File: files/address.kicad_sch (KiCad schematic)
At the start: 4 parts, among them J1 VLB_slot, U1 86C325

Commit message: initial PCB routed
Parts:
- added C14: 0.1uF, Capacitor_SMD:C_0805_2012Metric_Pad1.18x1.45mm_HandSolder, symbol Device:C
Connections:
- net GND: now also C14.2
- net at R5.1, U1.193 (~{SRESET}): now also C14.1
- net IRQ2: no longer names the net of JP2.1 (Pin_1)
- no-connect marks 8 -> 9
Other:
- moved on the sheet: R5
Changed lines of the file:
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@@
 (kicad_sch (version 20230121) (generator eeschema)
   (paper "A4")
+  (junction (at 190.5 133.35) (diameter 0) (color 0 0 0 0)
+  )
   (no_connect (at 39.37 85.09))
   (no_connect (at 72.39 85.09))
@@
   (no_connect (at 66.04 187.96))
   (no_connect (at 57.15 85.09))
+  (no_connect (at 191.77 100.33))
   (wire (pts (xy 20.32 130.81) (xy 27.94 130.81))
     (stroke (width 0) (type default))
@@
     (stroke (width 0) (type default))
   )
+  (wire (pts (xy 190.5 133.35) (xy 190.5 137.16))
+    (stroke (width 0) (type default))
+  )
   (wire (pts (xy 158.75 182.88) (xy 149.86 182.88))
     (stroke (width 0) (type default))
@@
     (stroke (width 0) (type default))
   )
-  (wire (pts (xy 193.04 133.35) (xy 201.93 133.35))
+  (wire (pts (xy 186.69 133.35) (xy 190.5 133.35))
     (stroke (width 0) (type default))
   )
@@
     (stroke (width 0) (type default))
   )
-  (wire (pts (xy 185.42 100.33) (xy 191.77 100.33))
-    (stroke (width 0) (type default))
-  )
   (wire (pts (xy 158.75 185.42) (xy 149.86 185.42))
     (stroke (width 0) (type default))
@@
     (stroke (width 0) (type default))
   )
-  (wire (pts (xy 177.8 133.35) (xy 185.42 133.35))
+  (wire (pts (xy 171.45 133.35) (xy 179.07 133.35))
     (stroke (width 0) (type default))
   )
@@
     (stroke (width 0) (type default))
   )
+  (wire (pts (xy 190.5 133.35) (xy 201.93 133.35))
+    (stroke (width 0) (type default))
+  )
   (wire (pts (xy 67.31 80.01) (xy 67.31 85.09))
     (stroke (width 0) (type default))
@@
     (effects (font (size 1.27 1.27)) (justify right bottom))
   )
-  (label "RST" (at 177.8 133.35 0) (fields_autoplaced)
+  (label "RST" (at 171.45 133.35 0) (fields_autoplaced)
     (effects (font (size 1.27 1.27)) (justify left bottom))
   )
@@
     (effects (font (size 1.27 1.27)) (justify right bottom))
   )
-  (hierarchical_label "IRQ2" (shape input) (at 185.42 100.33 180) (fields_autoplaced)
-    (effects (font (size 1.27 1.27)) (justify right))
-  )
-  (symbol (lib_id "Device:R") (at 189.23 133.35 270) (mirror x) (unit 1)
+  (symbol (lib_id "Device:R") (at 182.88 133.35 270) (mirror x) (unit 1)
     (in_bom yes) (on_board yes) (dnp no)
-    (property "Reference" "R5" (at 187.96 128.27 90)
+    (property "Reference" "R5" (at 181.61 128.27 90)
       (effects (font (size 1.27 1.27)) (justify left))
     )
-    (property "Value" "100R" (at 187.325 130.81 90)
+    (property "Value" "100R" (at 180.975 130.81 90)
       (effects (font (size 1.27 1.27)) (justify left))
     )
-    (property "Footprint" "Resistor_SMD:R_0805_2012Metric_Pad1.20x1.40mm_HandSolder" (at 189.23 135.128 90)
+    (property "Footprint" "Resistor_SMD:R_0805_2012Metric_Pad1.20x1.40mm_HandSolder" (at 182.88 135.128 90)
       (effects (font (size 1.27 1.27)) hide)
     )
-    (property "Datasheet" "~" (at 189.23 133.35 0)
+    (property "Datasheet" "~" (at 182.88 133.35 0)
       (effects (font (size 1.27 1.27)) hide)
     )
@@
     )
   )
+  (symbol (lib_id "Device:C") (at 190.5 140.97 0) (unit 1)
+    (in_bom yes) (on_board yes) (dnp no)
+    (property "Reference" "C14" (at 184.15 138.43 0)
+      (effects (font (size 1.27 1.27)) (justify left))
+    )
+    (property "Value" "0.1uF" (at 182.88 143.51 0)
+      (effects (font (size 1.27 1.27)) (justify left))
+    )
+    (property "Footprint" "Capacitor_SMD:C_0805_2012Metric_Pad1.18x1.45mm_HandSolder" (at 191.4652 144.78 0)
+      (effects (font (size 1.27 1.27)) hide)
+    )
+    (property "Datasheet" "~" (at 190.5 140.97 0)
+      (effects (font (size 1.27 1.27)) hide)
+    )
+    (pin "1")
+    (pin "2")
+    (instances
+      (project "virge-vlb"
+        (path "/e8216711-86b5-4276-82f4-4c7ed22b9a9c"
+          (reference "C14") (unit 1)
+        )
+        (path "/e8216711-86b5-4276-82f4-4c7ed22b9a9c/9321f466-5ac6-411a-b039-07fb7f0cdeaa"
+          (reference "C15") (unit 1)
+        )
+      )
+    )
+  )
   (symbol (lib_id "power:GND") (at 27.94 179.07 0) (unit 1)
     (in_bom yes) (on_board yes) (dnp no) (fields_autoplaced)
@@
         )
       )
+    )
+  )
+  (symbol (lib_id "power:GND") (at 190.5 144.78 0) (unit 1)
+    (in_bom yes) (on_board yes) (dnp no) (fields_autoplaced)
+    (property "Reference" "#PWR05" (at 190.5 151.13 0)
+      (effects (font (size 1.27 1.27)) hide)
+    )
+    (property "Value" "GND" (at 190.5 149.86 0)
+      (effects (font (size 1.27 1.27)))
+    )
+    (property "Footprint" "" (at 190.5 144.78 0)
+      (effects (font (size 1.27 1.27)) hide)
+    )
+    (property "Datasheet" "" (at 190.5 144.78 0)
+      (effects (font (size 1.27 1.27)) hide)
+    )
+    (pin "1")
+    (instances
+      (project "virge-vlb"
+        (path "/e8216711-86b5-4276-82f4-4c7ed22b9a9c/485e825d-a3d2-4e3d-9ea7-d005dd511bf5"
+          (reference "#PWR05") (unit 1)
+        )
+        (path "/e8216711-86b5-4276-82f4-4c7ed22b9a9c/9321f466-5ac6-411a-b039-07fb7f0cdeaa"
+          (reference "#PWR046") (unit 1)
+        )
+      )

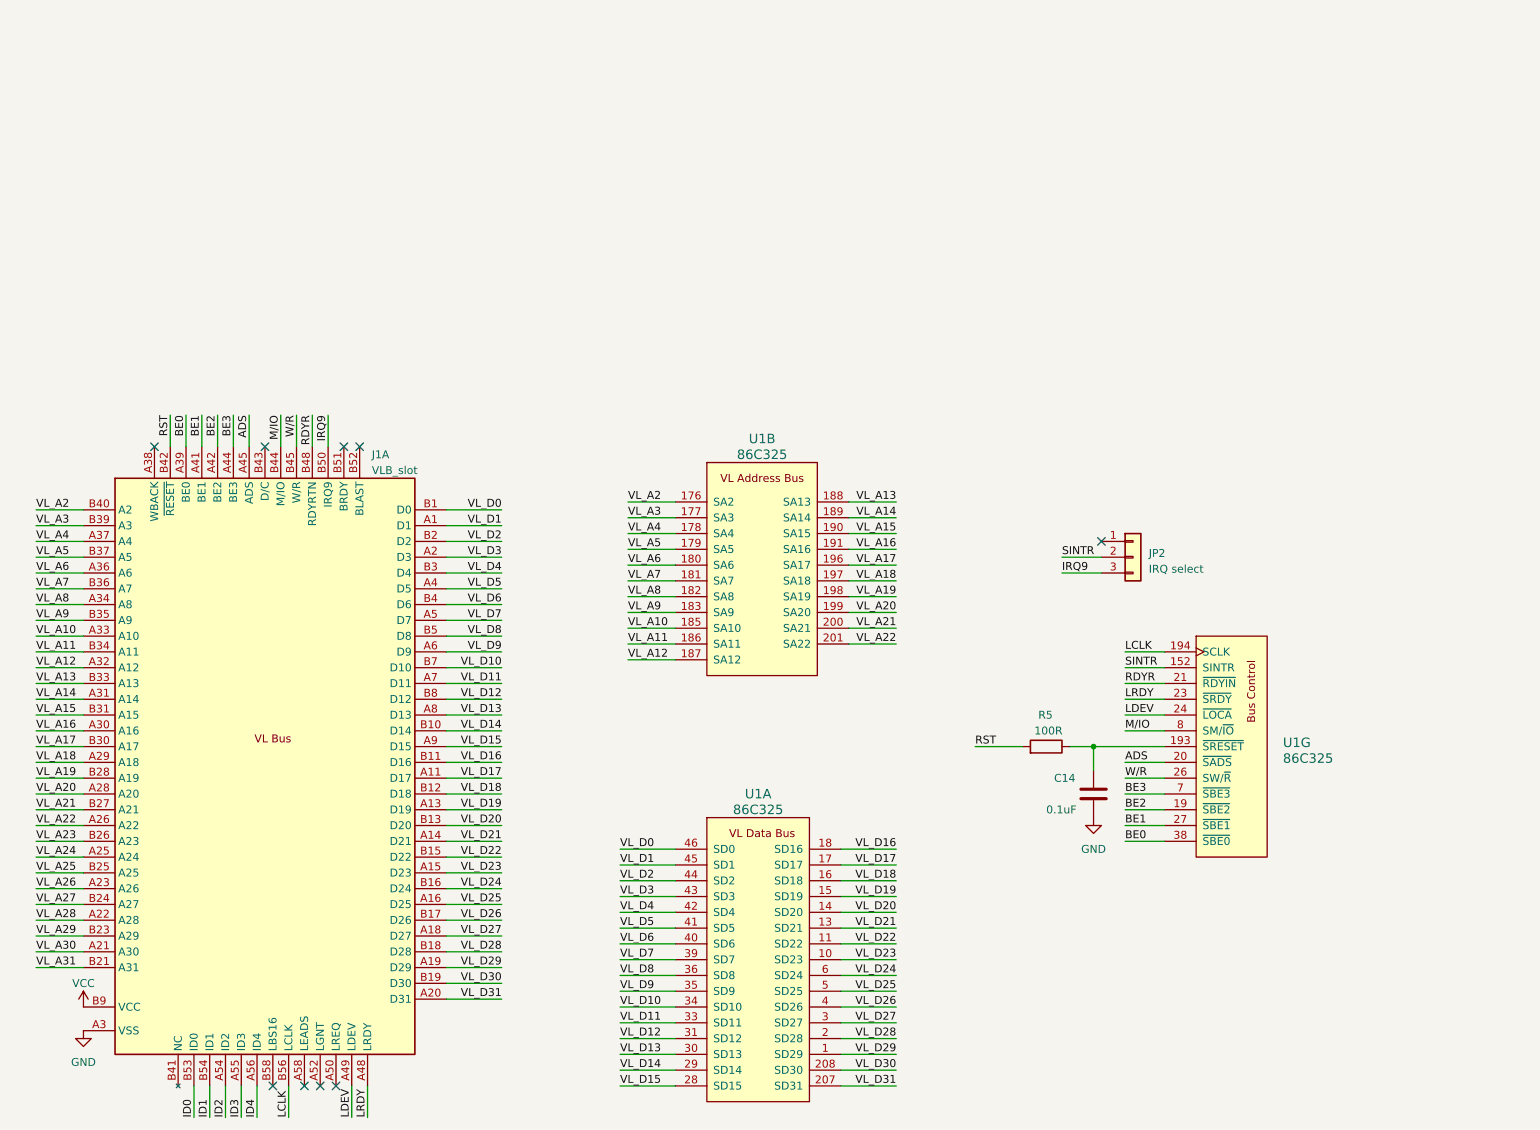
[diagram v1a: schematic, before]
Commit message: added SAUP decoding, adjusted VGA conn.
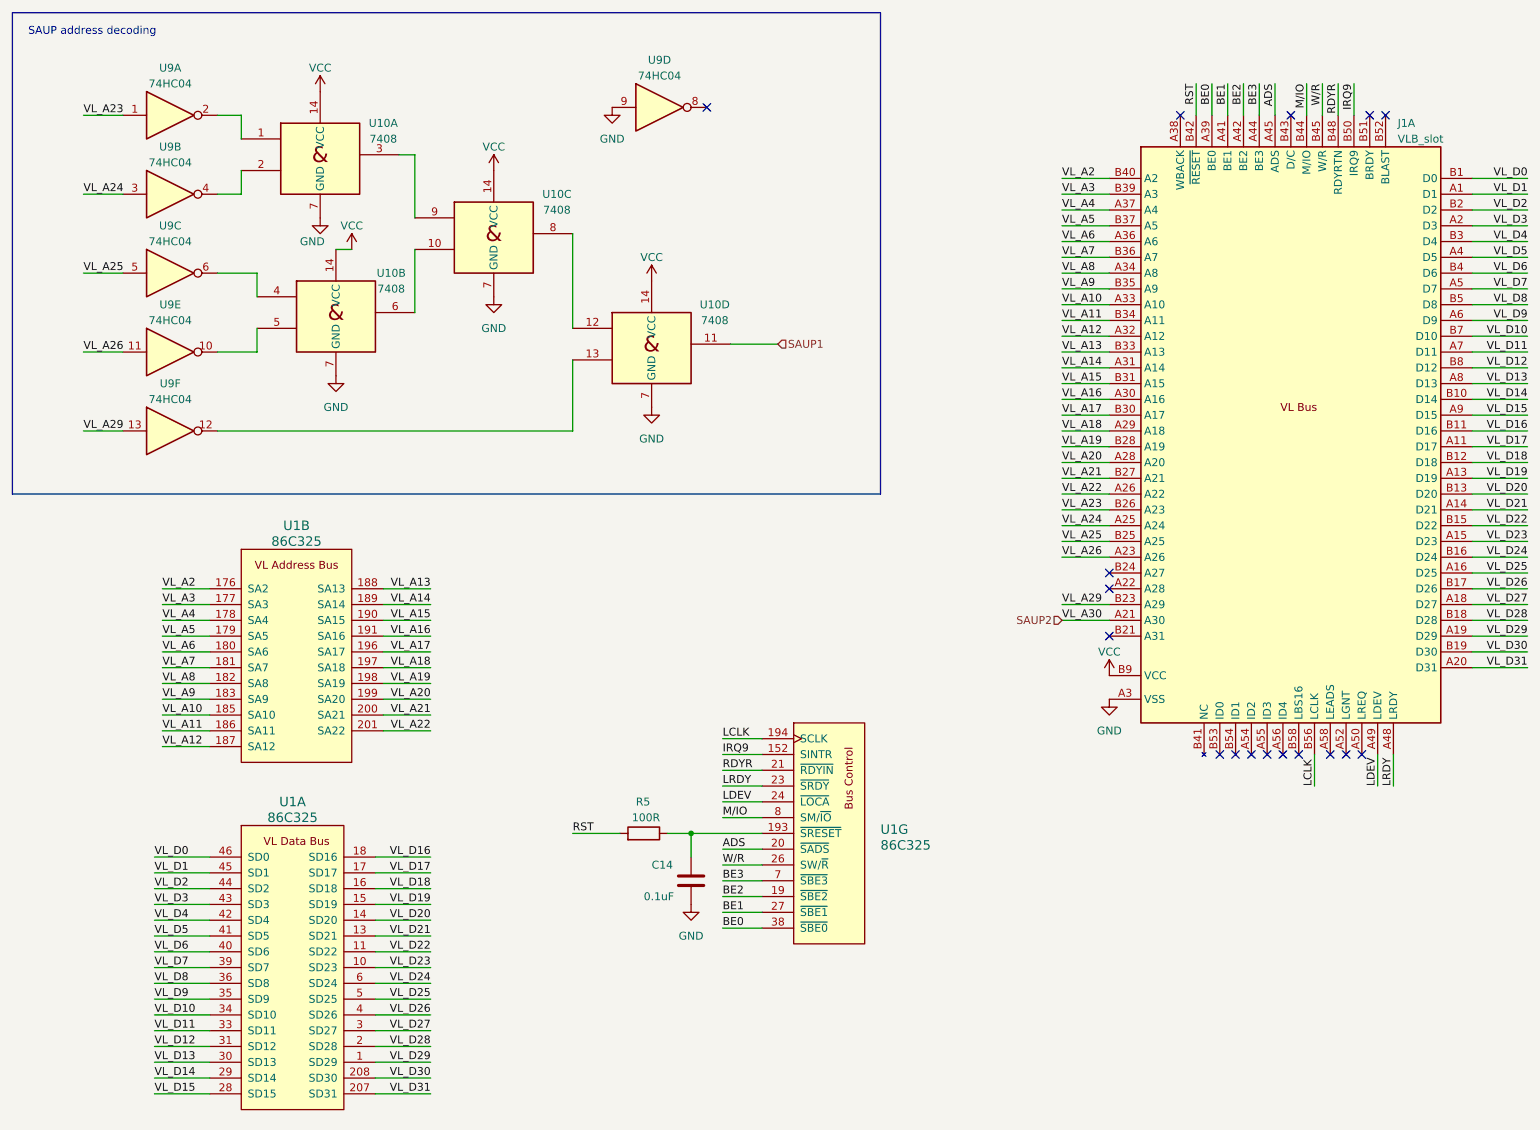
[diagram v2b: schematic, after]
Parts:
- removed JP2: IRQ select, Connector_PinHeader_2.54mm:PinHeader_1x03_P2.54mm_Vertical, symbol Connector_Generic:Conn_01x03
- added U10: 7408, Package_SO:SO-14_3.9x8.65mm_P1.27mm, symbol 74xx_IEEE:7408
- added U9: 74HC04, Package_SO:SO-14_3.9x8.65mm_P1.27mm, symbol 74xx:74HC04
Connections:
- net SINTR is gone; now on net IRQ9: U1.152 (SINTR)
- net GND: now also U10.7 (GND), U10.7 (GND), U10.7 (GND), U10.7 (GND), U9.9
- net VCC: now also U10.14 (VCC), U10.14 (VCC), U10.14 (VCC), U10.14 (VCC)
- net VL_A23: now also U9.1
- net VL_A24: now also U9.3
- net VL_A25: now also U9.5
- net VL_A26: now also U9.11
- net VL_A29: now also U9.13
- net ID0: no longer names the net of J1.B53 (ID0)
- net ID1: no longer names the net of J1.B54 (ID1)
- net ID2: no longer names the net of J1.A54 (ID2)
- net ID3: no longer names the net of J1.A55 (ID3)
- net ID4: no longer names the net of J1.A56 (ID4)
- net VL_A27: no longer names the net of J1.B24 (A27)
- net VL_A28: no longer names the net of J1.A22 (A28)
- net VL_A30 renamed SAUP2
- net VL_A31: no longer names the net of J1.B21 (A31)
- new net: U10.13, U9.12
- new net: U10.10, U10.6
- new net: U10.12, U10.8
- new net: U10.3, U10.9
- new net: U10.1, U9.2
- new net: U10.2, U9.4
- new net: U10.4, U9.6
- new net: U10.5, U9.10
- new net SAUP1: U10.11
- no-connect marks 9 -> 17
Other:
- note added: "SAUP address decoding"
- moved on the sheet: C14, J1A, R5, U1A, U1B, U1G

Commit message: added address jumpers
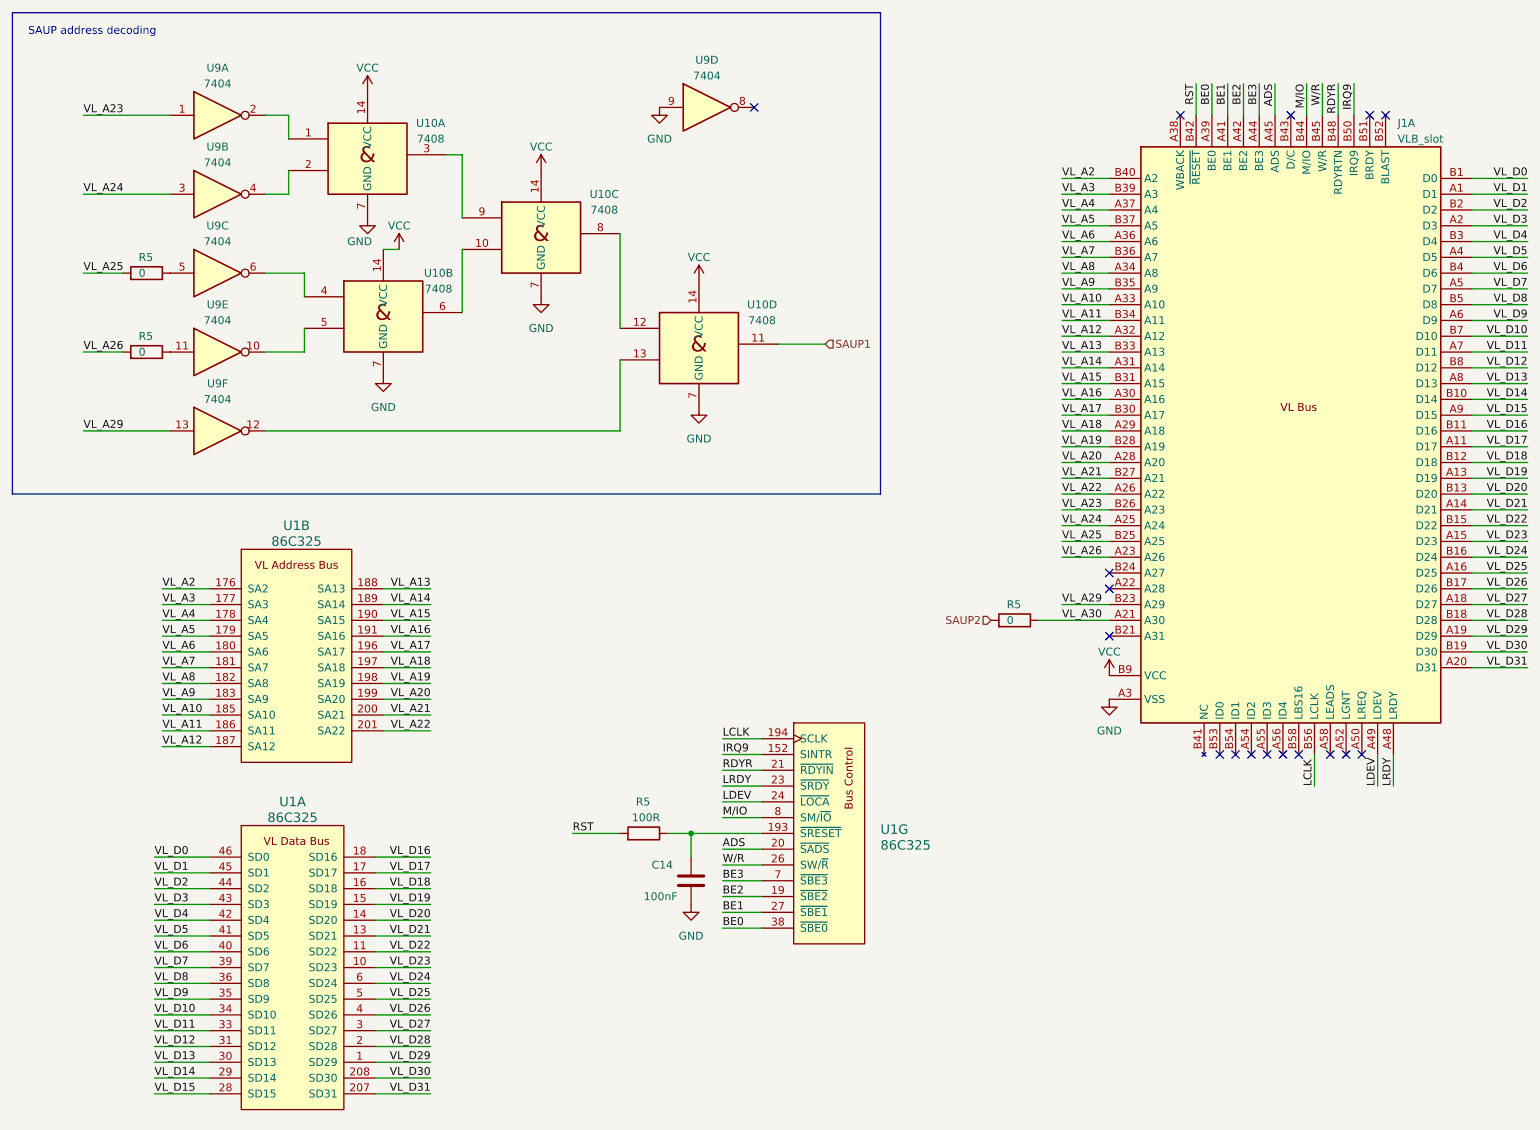
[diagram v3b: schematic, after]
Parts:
- added R5 (x3): 0, Resistor_SMD:R_0805_2012Metric_Pad1.20x1.40mm_HandSolder, symbol Device:R
- C14: value 0.1uF -> 100nF
- U9: value 74HC04 -> 7404
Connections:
- net SAUP2: now also R5.2; no longer J1.A21 (A30)
- net VL_A25: now also R5.2; no longer U9.5
- net VL_A26: now also R5.2; no longer U9.11
- new net: R5.1, U9.11
- new net: R5.1, U9.5
- new net VL_A30: J1.A21 (A30), R5.1
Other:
- moved on the sheet: U10A, U10B, U10C, U10D, U9A, U9B, U9C, U9D, U9E, U9F

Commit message: Board review changes 2023-07-06
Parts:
- added C19, C20: 100nF, Capacitor_SMD:C_0805_2012Metric_Pad1.18x1.45mm_HandSolder, symbol Device:C
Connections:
- net GND: now also C19.2, C20.2; no longer U9.9
- net VCC: now also U9.9, C19.1, C20.1
- net VL_A29_O: now reaches U10.13, U9.12
- net VL_A25+A26: now reaches U10.10, U10.6
- net VL_A23-A26: now reaches U10.12, U10.8
- net VL_A23+A24: now reaches U10.3, U10.9
- net VL_A23_O: now reaches U10.1, U9.2
- net VL_A24_O: now reaches U10.2, U9.4
- net VL_A25_O: now reaches U10.4, U9.6
- net VL_A26_O: now reaches U10.5, U9.10
- no-connect marks 17 -> 18
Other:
- note added: "Chip defaults to IRQ9"

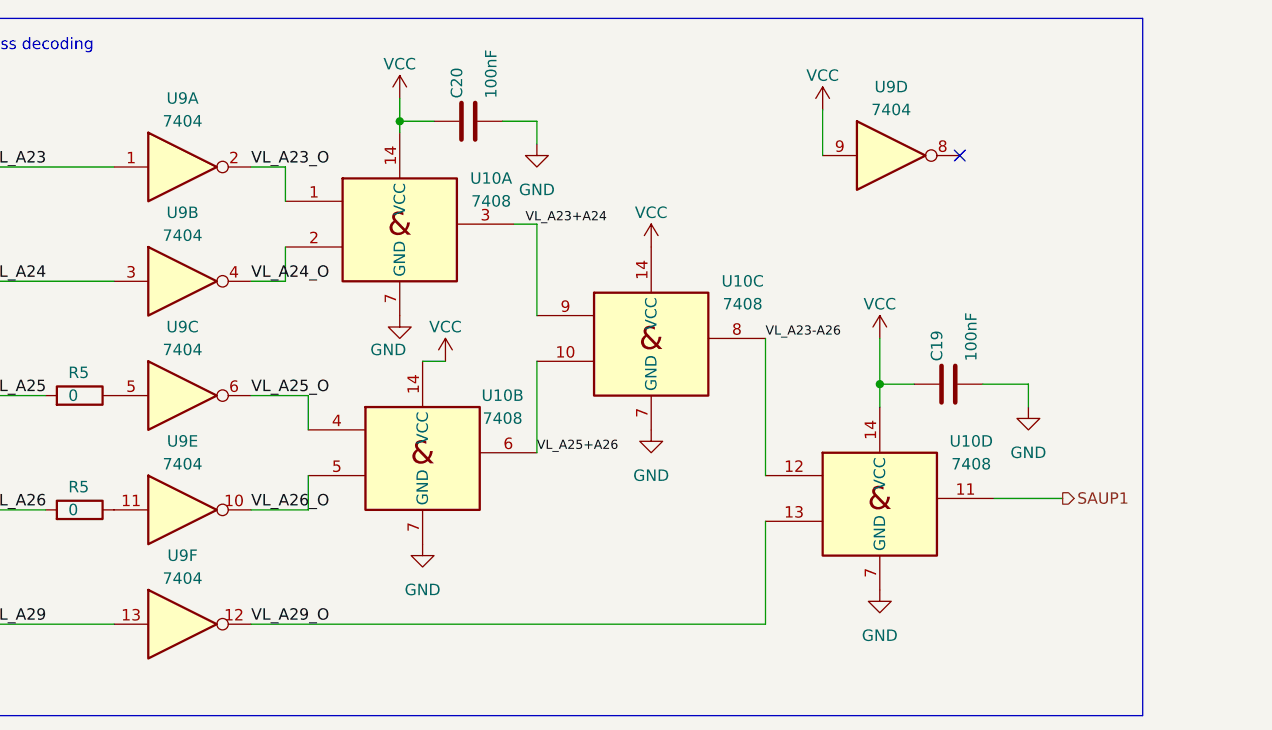
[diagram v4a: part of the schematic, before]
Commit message: fixed some clearance issues, fixed S3 logo, fixed annotations
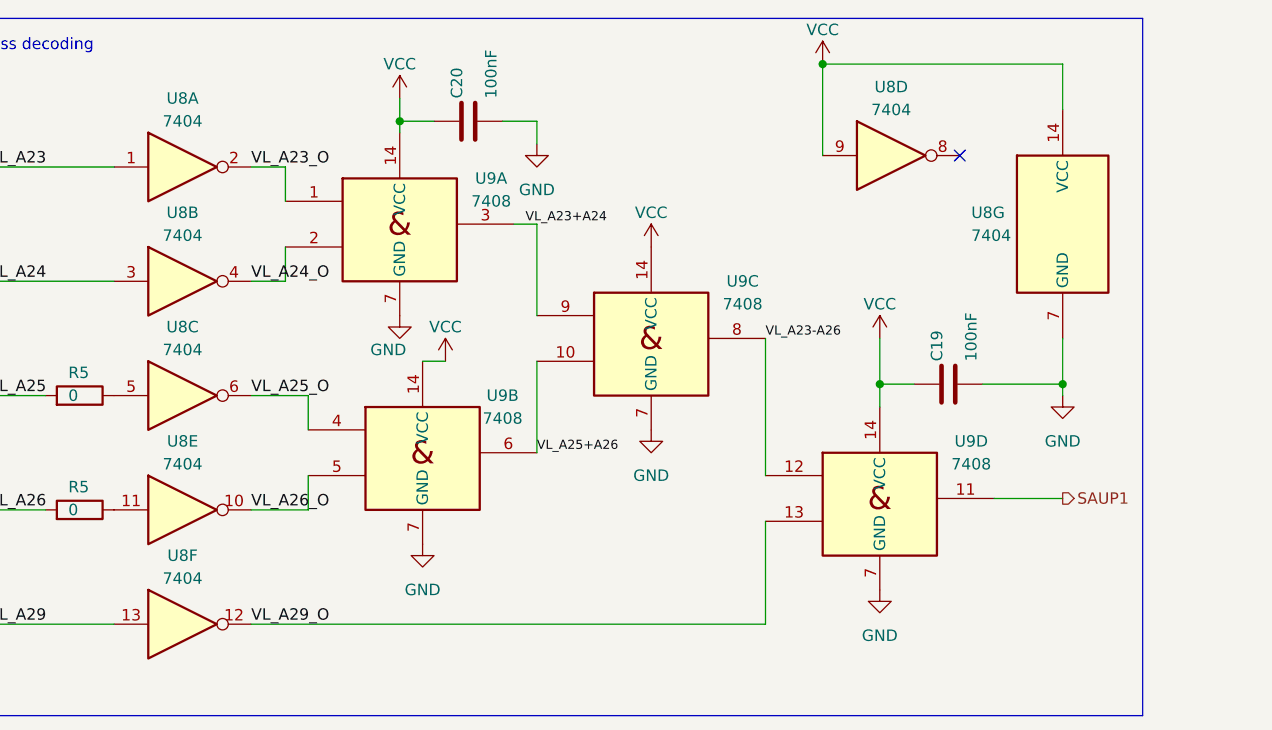
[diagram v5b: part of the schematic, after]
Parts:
- added unit 7 of U8
- renumbered U9 to U8, U10 to U9
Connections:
- net GND: now also U8.7 (GND)
- net VCC: now also U8.14 (VCC)
